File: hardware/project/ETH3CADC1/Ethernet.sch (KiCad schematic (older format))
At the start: 43 parts, among them U601 LAN8742A, U602 LC03-3.3, U603 LC03-3.3, Y601 NX5032GA-25.000M-LN-CD-1

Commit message: PCB layout
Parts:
- C606, C607: footprint Capacitor_SMD:C_0603_1608Metric_Pad1.08x0.95mm_HandSolder -> Capacitor_SMD:C_0402_1005Metric_Pad0.74x0.62mm_HandSolder
- R620, R621: footprint Resistor_SMD:R_0402_1005Metric_Pad0.72x0.64mm_HandSolder -> Resistor_SMD:R_0603_1608Metric_Pad0.98x0.95mm_HandSolder
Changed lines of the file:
@@
 $Descr A4 11693 8268
 encoding utf-8
-Sheet 6 13
+Sheet 6 15
 Title "Ethernet"
 Date "2020-03-07"
@@
 F 0 "C606" H 2765 1996 50  0000 L CNN
 F 1 "1u" H 2765 1905 50  0000 L CNN
-F 2 "Capacitor_SMD:C_0603_1608Metric_Pad1.08x0.95mm_HandSolder" H 2688 1800 50  0001 C CNN
+F 2 "Capacitor_SMD:C_0402_1005Metric_Pad0.74x0.62mm_HandSolder" H 2688 1800 50  0001 C CNN
 F 3 "~" H 2650 1950 50  0001 C CNN
 	1    2650 1950
@@
 F 0 "R620" H 8920 3896 50  0000 L CNN
 F 1 "75/1%" H 8920 3805 50  0000 L CNN
-F 2 "Resistor_SMD:R_0402_1005Metric_Pad0.72x0.64mm_HandSolder" V 8780 3850 50  0001 C CNN
+F 2 "Resistor_SMD:R_0603_1608Metric_Pad0.98x0.95mm_HandSolder" V 8780 3850 50  0001 C CNN
 F 3 "~" H 8850 3850 50  0001 C CNN
 	1    8850 3850
@@
 F 0 "R621" H 9420 3896 50  0000 L CNN
 F 1 "75/1%" H 9420 3805 50  0000 L CNN
-F 2 "Resistor_SMD:R_0402_1005Metric_Pad0.72x0.64mm_HandSolder" V 9280 3850 50  0001 C CNN
+F 2 "Resistor_SMD:R_0603_1608Metric_Pad0.98x0.95mm_HandSolder" V 9280 3850 50  0001 C CNN
 F 3 "~" H 9350 3850 50  0001 C CNN
 	1    9350 3850
@@
 F 0 "C607" H 3865 1296 50  0000 L CNN
 F 1 "1u" H 3865 1205 50  0000 L CNN
-F 2 "Capacitor_SMD:C_0603_1608Metric_Pad1.08x0.95mm_HandSolder" H 3788 1100 50  0001 C CNN
+F 2 "Capacitor_SMD:C_0402_1005Metric_Pad0.74x0.62mm_HandSolder" H 3788 1100 50  0001 C CNN
 F 3 "~" H 3750 1250 50  0001 C CNN
 	1    3750 1250

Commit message: PCB modifications
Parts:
- FB601: footprint Inductor_SMD:L_0805_2012Metric_Pad1.15x1.40mm_HandSolder -> Inductor_SMD:L_0603_1608Metric_Pad1.05x0.95mm_HandSolder
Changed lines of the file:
@@
 F 0 "FB601" V 3226 1050 50  0000 C CNN
 F 1 "742792031" V 3317 1050 50  0000 C CNN
-F 2 "Inductor_SMD:L_0805_2012Metric_Pad1.15x1.40mm_HandSolder" V 3430 1050 50  0001 C CNN
+F 2 "Inductor_SMD:L_0603_1608Metric_Pad1.05x0.95mm_HandSolder" V 3430 1050 50  0001 C CNN
 F 3 "~" H 3500 1050 50  0001 C CNN
 	1    3500 1050

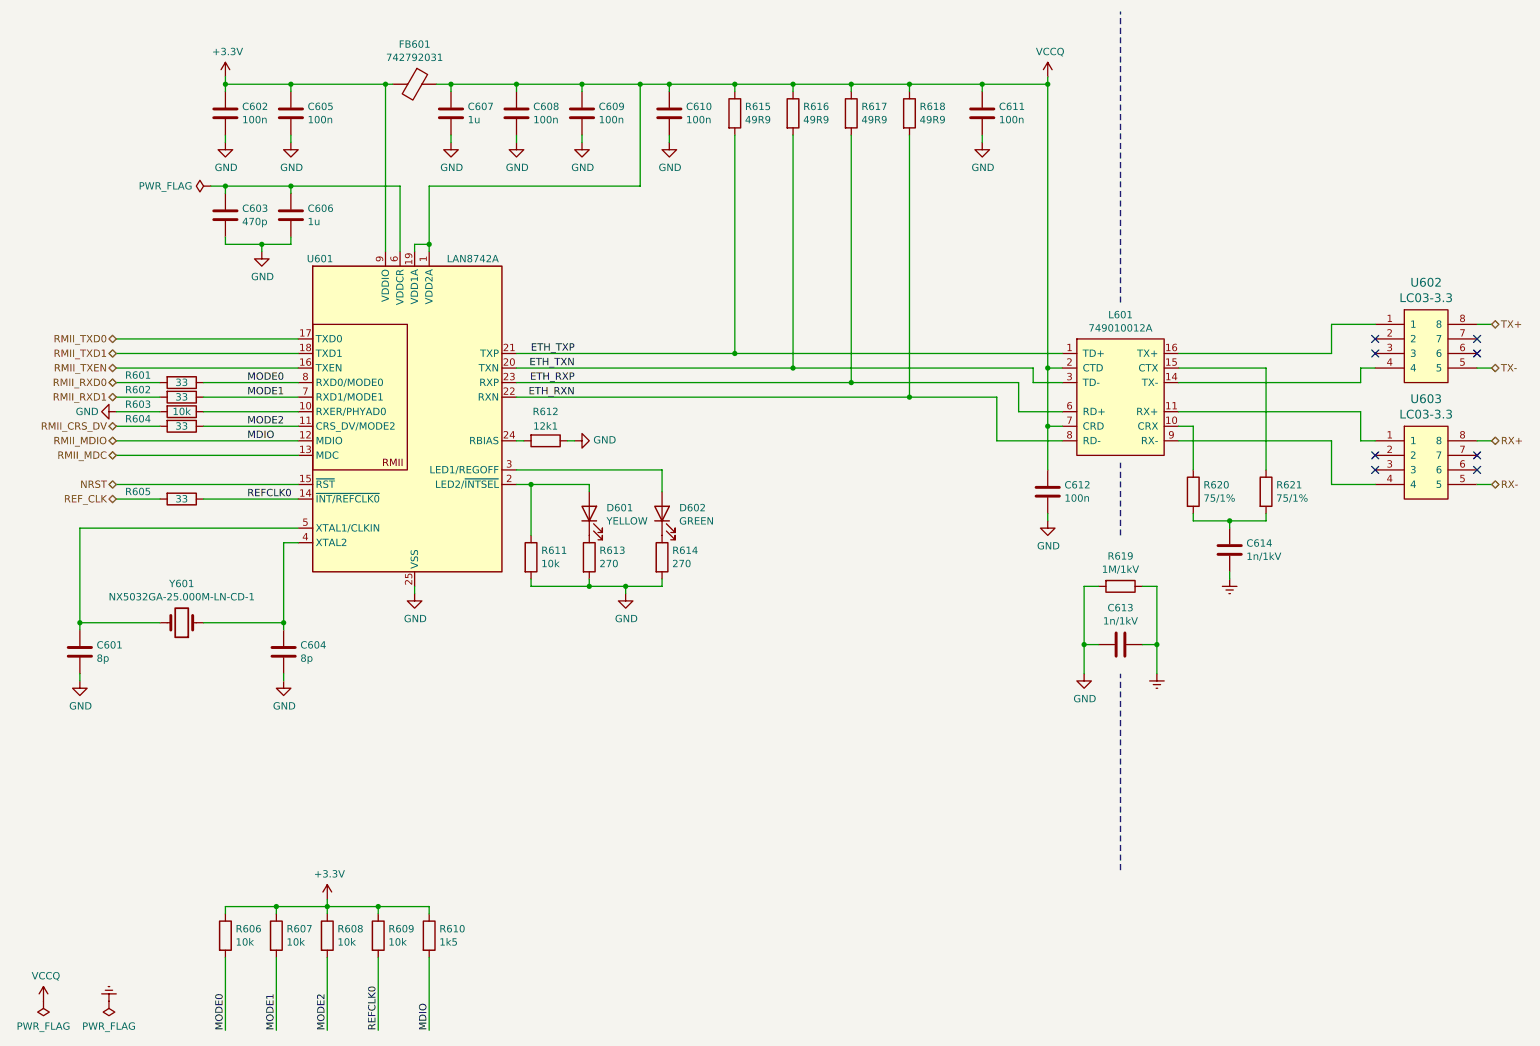
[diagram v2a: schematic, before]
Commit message: SDRAM works, thanks to the website https://medium.com/@pjinwoo123/stm32h7-external-sdram-evaluation-board-cc72444898d8 . Modified the code to work with SDRAM BANK2. SCPI library works.
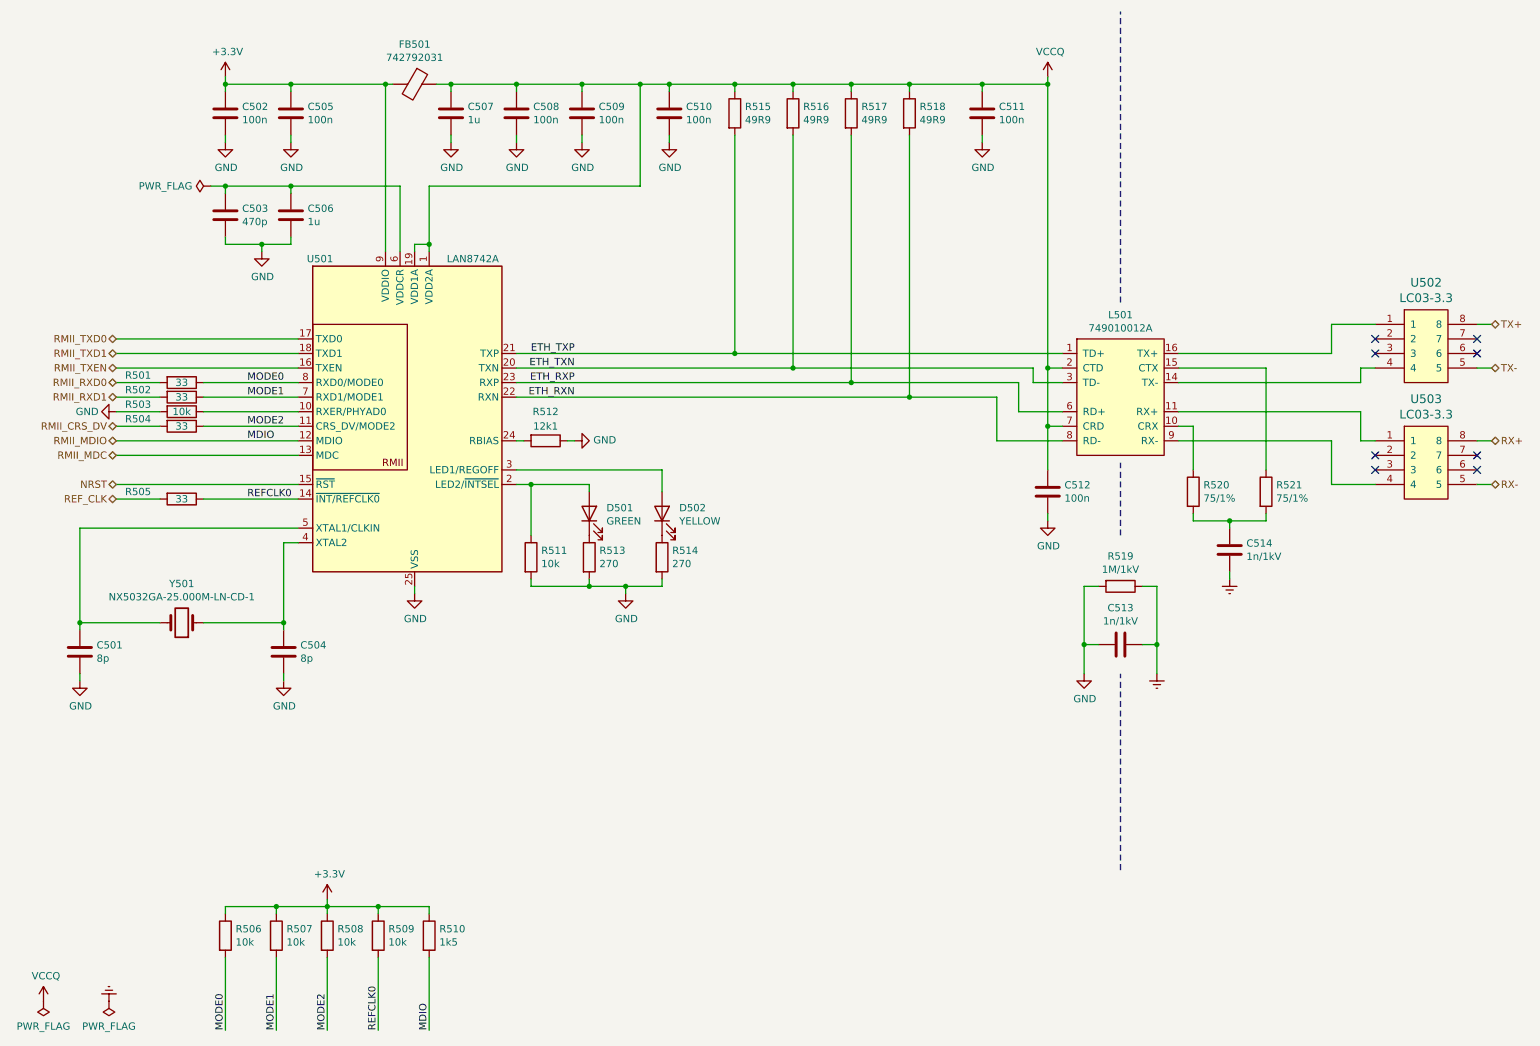
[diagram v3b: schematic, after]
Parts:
- D501: renamed from D601; value YELLOW -> GREEN
- D502: renamed from D602; value GREEN -> YELLOW
- renumbered C601 to C501, C602 to C502, C603 to C503, C604 to C504, C605 to C505, C606 to C506, C607 to C507, C608 to C508, C609 to C509, C610 to C510, C611 to C511, C612 to C512, C613 to C513, C614 to C514, FB601 to FB501, L601 to L501, R601 to R501, R602 to R502, R603 to R503, R604 to R504, R605 to R505, R606 to R506, R607 to R507, R608 to R508, R609 to R509, R610 to R510, R611 to R511, R612 to R512, R613 to R513, R614 to R514, R615 to R515, R616 to R516, R617 to R517, R618 to R518, R619 to R519, R620 to R520, R621 to R521, U601 to U501, U602 to U502, U603 to U503, Y601 to Y501

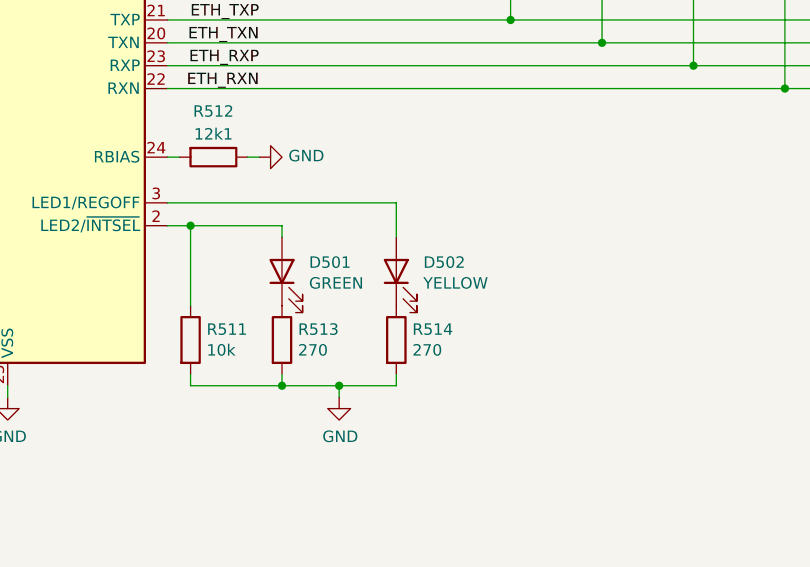
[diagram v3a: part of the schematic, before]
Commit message: Added SDRAM to the linker file.
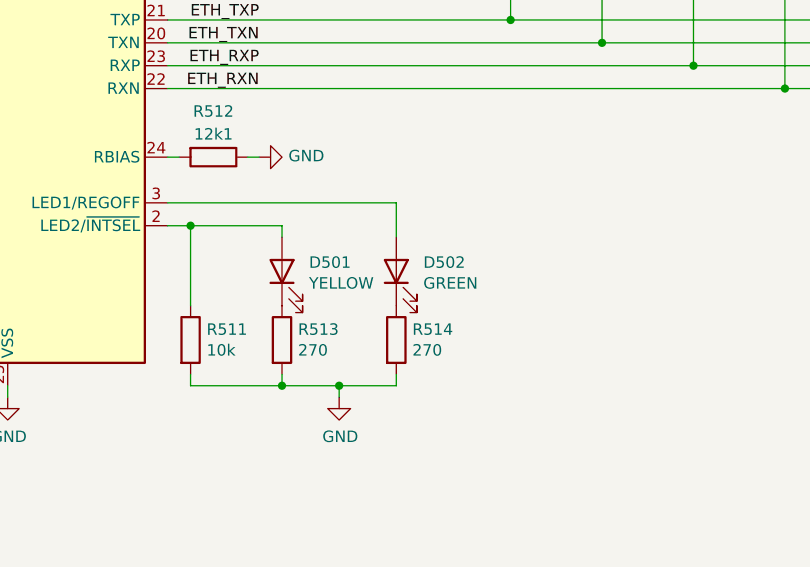
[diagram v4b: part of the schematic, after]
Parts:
- D501: value GREEN -> YELLOW
- D502: value YELLOW -> GREEN
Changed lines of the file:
@@
 $Descr A4 11693 8268
 encoding utf-8
-Sheet 6 13
+Sheet 5 13
 Title "Ethernet"
 Date "2020-03-07"
@@
 P 4700 4000
 F 0 "D501" V 4739 3882 50  0000 R CNN
-F 1 "GREEN" V 4648 3882 50  0000 R CNN
+F 1 "YELLOW" V 4648 3882 50  0000 R CNN
 F 2 "LED_SMD:LED_0603_1608Metric_Pad1.05x0.95mm_HandSolder" H 4700 4000 50  0001 C CNN
 F 3 "~" H 4700 4000 50  0001 C CNN
@@
 P 5200 4000
 F 0 "D502" V 5239 3882 50  0000 R CNN
-F 1 "YELLOW" V 5148 3882 50  0000 R CNN
+F 1 "GREEN" V 5148 3882 50  0000 R CNN
 F 2 "LED_SMD:LED_0603_1608Metric_Pad1.05x0.95mm_HandSolder" H 5200 4000 50  0001 C CNN
 F 3 "~" H 5200 4000 50  0001 C CNN
